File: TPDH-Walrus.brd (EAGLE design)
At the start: 16 x 39.9 mm, 45 parts, among them Q2 DMG3404, U1 MS5803-14BA, U2 SN65HVD33RHL, U4 MCP3421A3, U5 TPS79733, U6 MAX6070AAUT18, U7 TXS0102DQM

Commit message: add SDO for I2C
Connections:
- net MISO: now also U1.8
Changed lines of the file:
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@@
 <wire x1="3.4356" y1="20.9254" x2="3.4356" y2="20.40579375" width="0.254" layer="1"/>
 <wire x1="3.4356" y1="20.40579375" x2="4.26459375" y2="19.5768" width="0.254" layer="1"/>
-<wire x1="7.159" y1="37.762" x2="3.342" y2="21.019" width="0" layer="19" extent="1-1"/>
 <wire x1="3.342" y1="21.019" x2="3.342" y2="21.019" width="0.254" layer="1"/>
+<contactref element="U1" pad="8"/>
+<wire x1="8.263" y1="32.1095" x2="7.159" y2="37.762" width="0" layer="19" extent="1-1"/>
+<wire x1="3.342" y1="21.019" x2="8.263" y2="32.1095" width="0" layer="19" extent="1-1"/>
 </signal>
 <signal name="VTHERM-">

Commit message: Routed, DRC passed
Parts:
- moved JP1 20.7 mm to (11.2, 20.9), turned to 180 degrees
- moved R6 1.20 mm to (5.99, 12.3)
- moved R7 0.06 mm to (3.54, 13.4)
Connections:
- removed net N$15: U3.1
- new net N$1: U3.6
- net PG: now also U3.1; no longer U3.6
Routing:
- net MISO: track 3.70 -> 27.0 mm, vias 1 -> 3
- net SDA: track 31.9 -> 53.3 mm
- net GND: track 75.4 -> 92.9 mm, vias 4 -> 5
- net SPI-I2C-SWITCH: track 0.00 -> 15.0 mm, vias 0 -> 2
- net +3V3: track 76.4 -> 89.9 mm, vias 7 -> 10
- net PG: track 4.69 -> 15.9 mm
- net RX+: track 17.5 -> 16.7 mm
- net /RESET: track 28.0 -> 28.7 mm

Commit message: Partial ERC
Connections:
- removed net N$1: U3.6
- removed net N$10: U3.11
- removed net N$14: U3.2
- removed net N$2: U3.7
- removed net N$7: U3.5
- removed net N$8: U3.13
- removed net N$9: U3.4
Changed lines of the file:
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@@
 <wire x1="1.842" y1="22.019" x2="2.4356" y2="21.4254" width="0.254" layer="1"/>
-</signal>
-<signal name="N$8">
-<contactref element="U3" pad="13"/>
-</signal>
-<signal name="N$10">
-<contactref element="U3" pad="11"/>
-</signal>
-<signal name="N$2">
-<contactref element="U3" pad="7"/>
-</signal>
-<signal name="N$7">
-<contactref element="U3" pad="5"/>
-</signal>
-<signal name="N$9">
-<contactref element="U3" pad="4"/>
-</signal>
-<signal name="N$14">
-<contactref element="U3" pad="2"/>
 </signal>
 <signal name="SDA_HV">
@@
 <wire x1="13.335" y1="31.877" x2="14.732" y2="31.877" width="0.254" layer="16"/>
 </signal>
-<signal name="N$1">
-<contactref element="U3" pad="6"/>
-</signal>
 </signals>

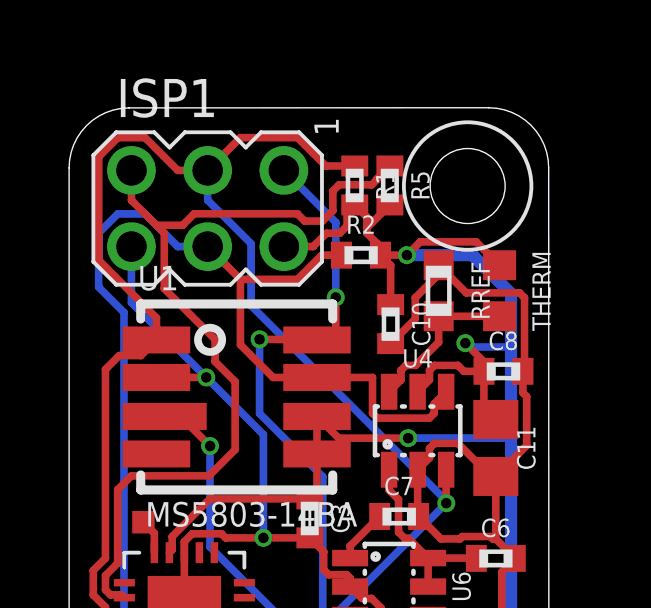
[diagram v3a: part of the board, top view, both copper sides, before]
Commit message: Fixed thermistor divider, removed SDO
Changed thermistor voltage to VRef rather than 3v3, and removed connection to SDO pin.
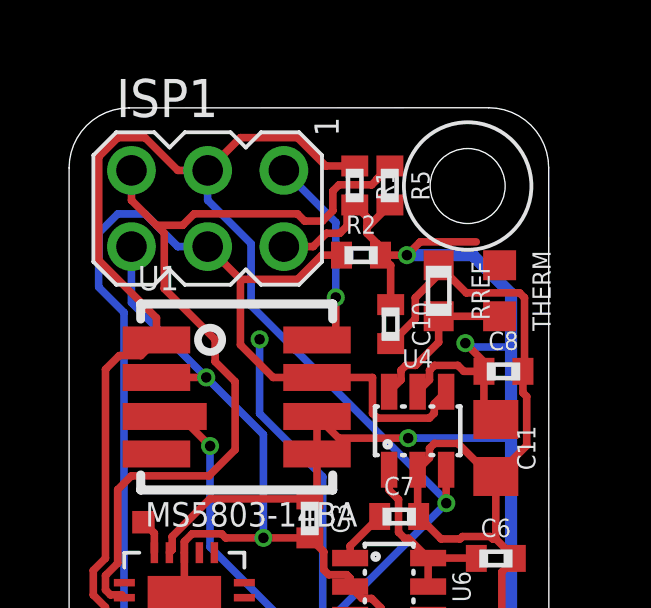
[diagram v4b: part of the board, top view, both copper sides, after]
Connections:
- net +3V3: no longer THERM.1
- net MISO: no longer U1.8
- net VREF: now also THERM.1
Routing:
- net MISO: track 27.0 -> 24.5 mm
- net +3V3: track 89.9 -> 88.8 mm

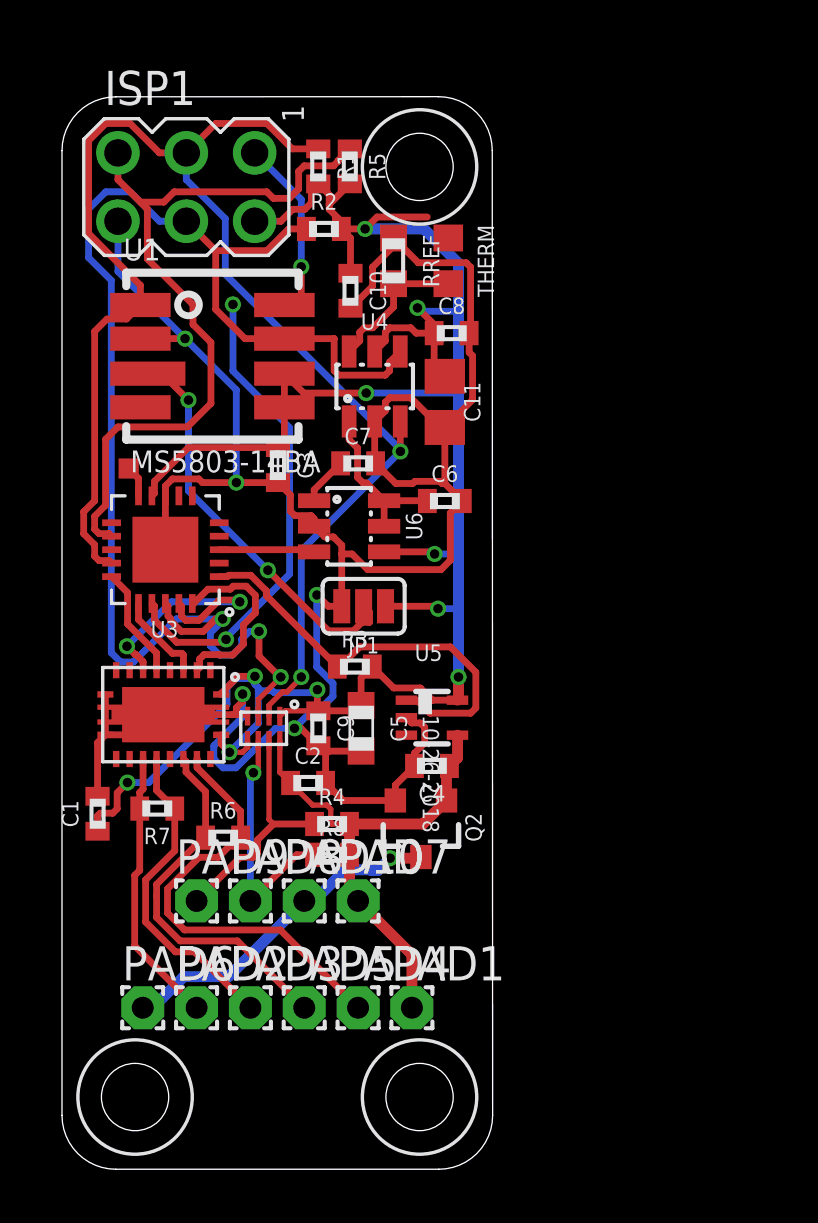
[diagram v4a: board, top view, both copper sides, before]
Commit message: Therm: reconnect and rearrange
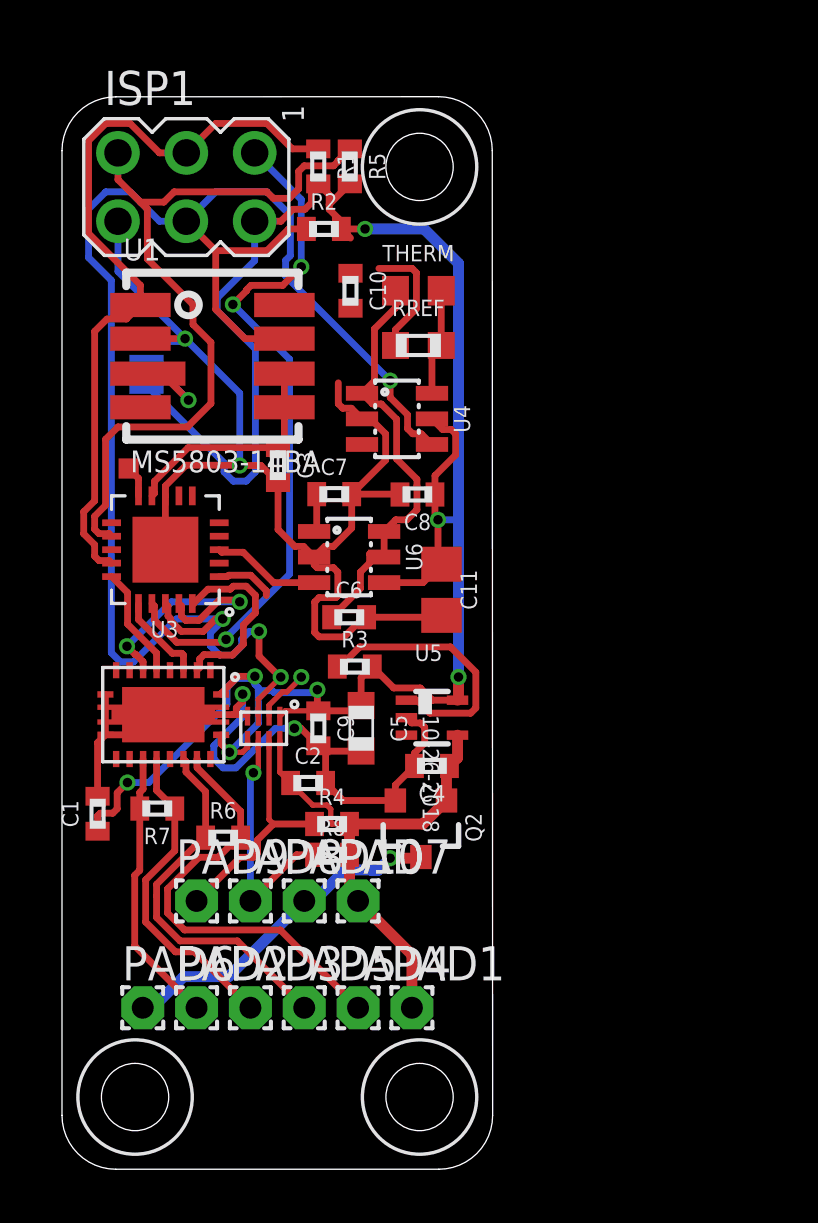
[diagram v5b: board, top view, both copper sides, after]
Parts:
- moved JP1 12.1 mm to (3.14, 29.9), flipped to the bottom, turned to 90 degrees
- moved C11 6.98 mm to (14.1, 21.5)
- moved C8 6.13 mm to (13.2, 25.1), turned to 180 degrees
- moved C6 5.59 mm to (10.7, 20.5)
- moved RREF 3.28 mm to (13.2, 30.6), turned to 0 degrees
- moved THERM 1.57 mm to (13.2, 32.6), turned to 0 degrees
- moved U4 1.46 mm to (12.4, 27.9), turned to 270 degrees
- moved C7 1.45 mm to (10.1, 25.1)
- moved U6 1.14 mm to (10.7, 22.7)
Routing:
- net SCL: track 56.0 -> 30.6 mm, vias 2 -> 1
- net GND: track 92.9 -> 78.2 mm, vias 5 -> 4
- net SPI-I2C-SWITCH: track 15.0 -> 4.24 mm, vias 2 -> 1
- net SDA: track 53.3 -> 63.0 mm, vias 3 -> 4
- net VREF: track 6.12 -> 15.7 mm
- net PG: track 15.9 -> 12.2 mm
- net +3V3: track 88.8 -> 91.4 mm, vias 10 -> 7
- net MISO: track 24.5 -> 26.1 mm
- net VTHERM-: track 5.42 -> 3.95 mm

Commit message: power pad update; uniform board outline
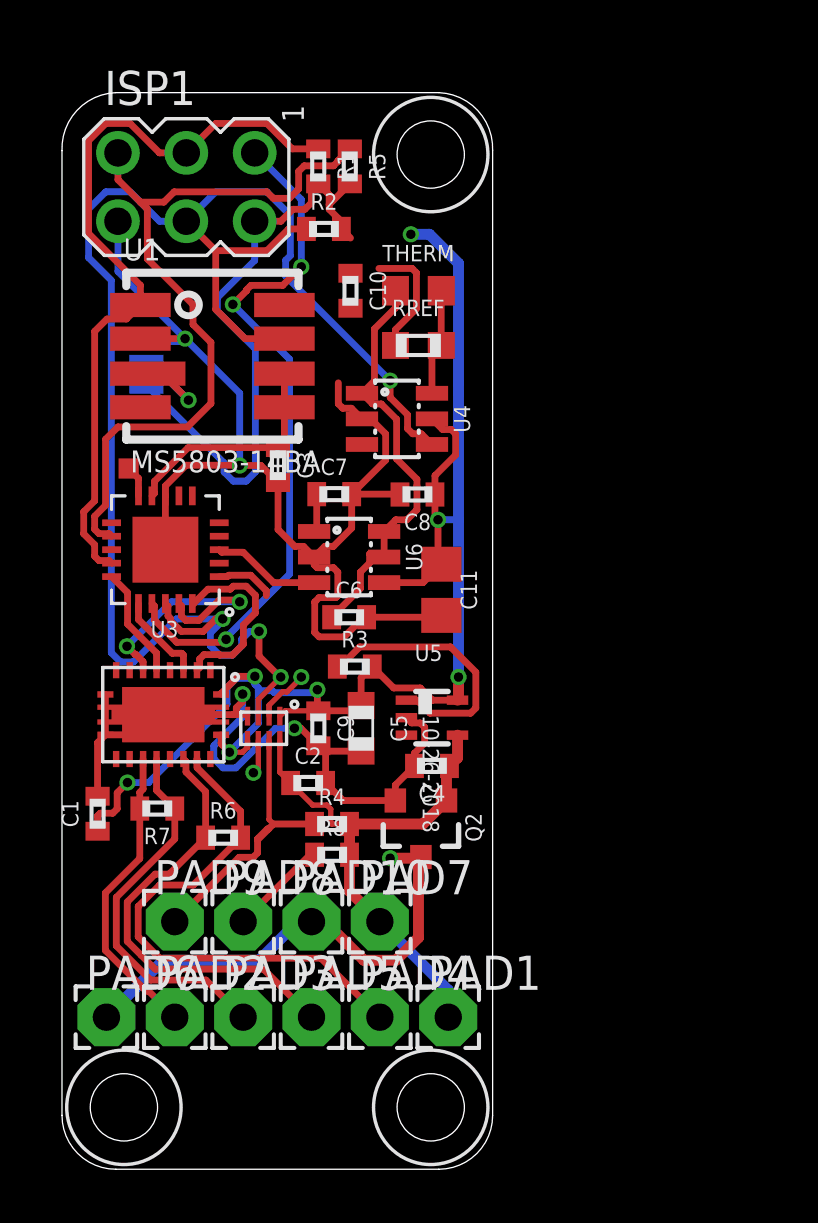
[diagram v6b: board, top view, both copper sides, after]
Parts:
- PAD1, PAD10, PAD2, PAD3, PAD4, PAD5, PAD6, PAD7, PAD8, PAD9: device wirepad:1,6/0,8 -> wirepad:2,15/1,0
- moved PAD6 1.39 mm to (1.65, 5.65)
- moved PAD1 1.39 mm to (14.3, 5.65)
- moved PAD7 1.12 mm to (11.8, 9.20)
- moved PAD9 1.12 mm to (4.19, 9.20)
- moved PAD4 0.88 mm to (11.8, 5.65)
- moved PAD2 0.88 mm to (4.19, 5.65)
- moved PAD10 0.82 mm to (9.27, 9.20)
- moved PAD8 0.82 mm to (6.73, 9.20)
- moved H1 0.62 mm to (13.7, 37.7)
- moved H3 0.56 mm to (2.30, 2.30)
- moved H2 0.56 mm to (13.7, 2.30)
- moved PAD3 0.44 mm to (6.73, 5.65)
- moved PAD5 0.44 mm to (9.27, 5.65)
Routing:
- net VIN-: track 12.7 -> 18.1 mm
- net SDA_HV: track 9.18 -> 5.12 mm
- net RX+: track 16.7 -> 19.8 mm
- net RX-: track 13.9 -> 16.6 mm
- net +3V3: track 91.4 -> 88.7 mm
- net TX-: track 12.0 -> 13.9 mm
- net SCL_HV: track 9.20 -> 10.9 mm
- net TX+: track 10.3 -> 11.3 mm
- net VIN+: track 19.2 -> 20.1 mm
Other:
- board size 16 x 39.9 mm -> 16 x 40 mm

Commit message: Update clearance, wire access; reroute
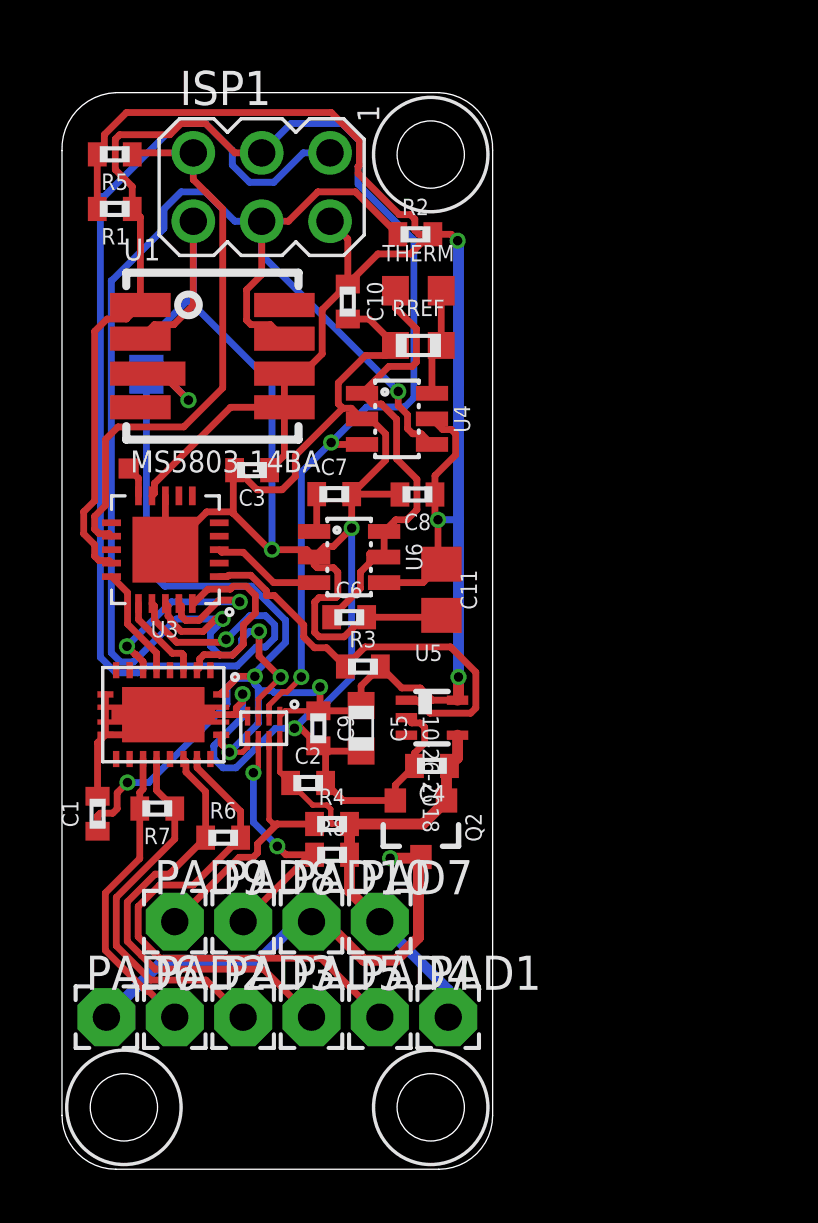
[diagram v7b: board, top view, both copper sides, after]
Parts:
- moved R5 8.74 mm to (1.96, 37.7), turned to 180 degrees
- moved R1 7.72 mm to (1.96, 35.7), turned to 180 degrees
- moved R2 3.41 mm to (13.1, 34.7)
- moved ISP1 2.80 mm to (7.42, 36.5)
- moved C3 0.98 mm to (7.06, 26.0), turned to 180 degrees
- moved C10 0.41 mm to (10.6, 32.2)
- moved R3 0.30 mm to (11.2, 18.7)
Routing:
- net SCL: track 30.6 -> 55.2 mm, vias 1 -> 2
- net +3V3: track 88.7 -> 111.1 mm
- net GND: track 78.2 -> 99.5 mm
- net MISO: track 26.1 -> 42.3 mm, vias 3 -> 1
- net /RESET: track 28.7 -> 20.9 mm
- net SDA_HV: track 5.12 -> 9.73 mm, vias 1 -> 2
- net PG: track 12.2 -> 16.2 mm
- net SDA: track 63.0 -> 60.0 mm
- net VREF: track 15.7 -> 16.9 mm
- net SCL_HV: track 10.9 -> 10.2 mm
